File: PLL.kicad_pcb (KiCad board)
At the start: 2 copper layers, 100 x 70 mm, 43 parts, among them J1 Vout, J10 VpfdB2_tp, J11 Vsq_tp, J12 Vfb_tp, J13 Ven_tp, J14 Vref_tp, J2 M=1, J3 M=2, J4 M=4, J5 Vcp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

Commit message: FINISH
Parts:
- added G***: LOGO, LOGO, F.Cu at (69.5, 98.1)
- added REF**: MountingHole_3.2mm_M3_Pad_TopBottom, MountingHole:MountingHole_3.2mm_M3_Pad_TopBottom, F.Cu at (61.0, 108.0)
- added REF**: MountingHole_3.2mm_M3_Pad_TopBottom, MountingHole:MountingHole_3.2mm_M3_Pad_TopBottom, F.Cu at (153.9, 108.0)
- added REF**: MountingHole_3.2mm_M3_Pad_TopBottom, MountingHole:MountingHole_3.2mm_M3_Pad_TopBottom, F.Cu at (61.1, 45.0)
- added REF**: MountingHole_3.2mm_M3_Pad_TopBottom, MountingHole:MountingHole_3.2mm_M3_Pad_TopBottom, F.Cu at (153.9, 45.1)
- moved J12 127.4 mm to (73.6, 84.8)
- moved U2 101.5 mm to (103.6, 90.0)
- moved D4 98.5 mm to (102.9, 55.0)
- moved C3 89.5 mm to (125.2, 60.5), turned to -90 degrees
- moved D2 88.7 mm to (102.9, 66.0)
- moved D3 87.5 mm to (110.5, 59.5), turned to 180 degrees
- moved R7 86.4 mm to (146.5, 53.5), turned to -90 degrees
- moved C2 84.7 mm to (129.6, 58.5), turned to 90 degrees
- moved R6 81.4 mm to (154.3, 64.8), turned to 180 degrees
- moved J11 80.7 mm to (118.5, 79.5)
- moved J8 80.6 mm to (111.0, 79.5)
- moved R10 79.6 mm to (113.4, 53.8)
- moved R5 78.6 mm to (150.0, 61.1), turned to 90 degrees
- moved D1 78.2 mm to (110.5, 70.5), turned to 180 degrees
- moved R12 75.8 mm to (99.2, 61.4), turned to 90 degrees
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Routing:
- net VCC: track 0.00 -> 320.4 mm
- net Net-(J12-Pin_1): track 0.00 -> 69.6 mm, vias 0 -> 1
- net Net-(J1-Pin_1): track 0.00 -> 63.8 mm
- net Net-(J8-Pin_1): track 0.00 -> 63.0 mm
- net Net-(J14-Pin_1): track 0.00 -> 52.0 mm
- net Net-(J13-Pin_1): track 0.00 -> 48.1 mm
- net Net-(J5-Pin_1): track 0.00 -> 46.0 mm
- net Net-(J10-Pin_1): track 0.00 -> 45.9 mm, vias 0 -> 2
- net Net-(J9-Pin_1): track 0.00 -> 33.3 mm
- net Net-(J3-Pin_1): track 0.00 -> 29.8 mm
- net Net-(U1A-~{R}): track 0.00 -> 29.4 mm
- net Net-(J4-Pin_1): track 0.00 -> 28.4 mm
- net Net-(Q2-G): track 0.00 -> 26.1 mm
- net Net-(D1-A): track 0.00 -> 24.6 mm
- net Net-(U3A--): track 0.00 -> 21.0 mm
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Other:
- outline, holes or cut-outs redrawn
- board text added: "5V"
- board text added: "CP"
- board text added: "Design of Analog Electronic Systems - Final Assignment RF Synthesizer (PLL)"
- board text added: "Divider"
- board text added: "Loop Filter"
- board text added: "PFD"
- board text added: "Schmitt Trigger"
- board text added: "VCO"
- board text removed: "Design of Analog Electronic Systems - Final Assingment RF Synthesizer (PLL)"

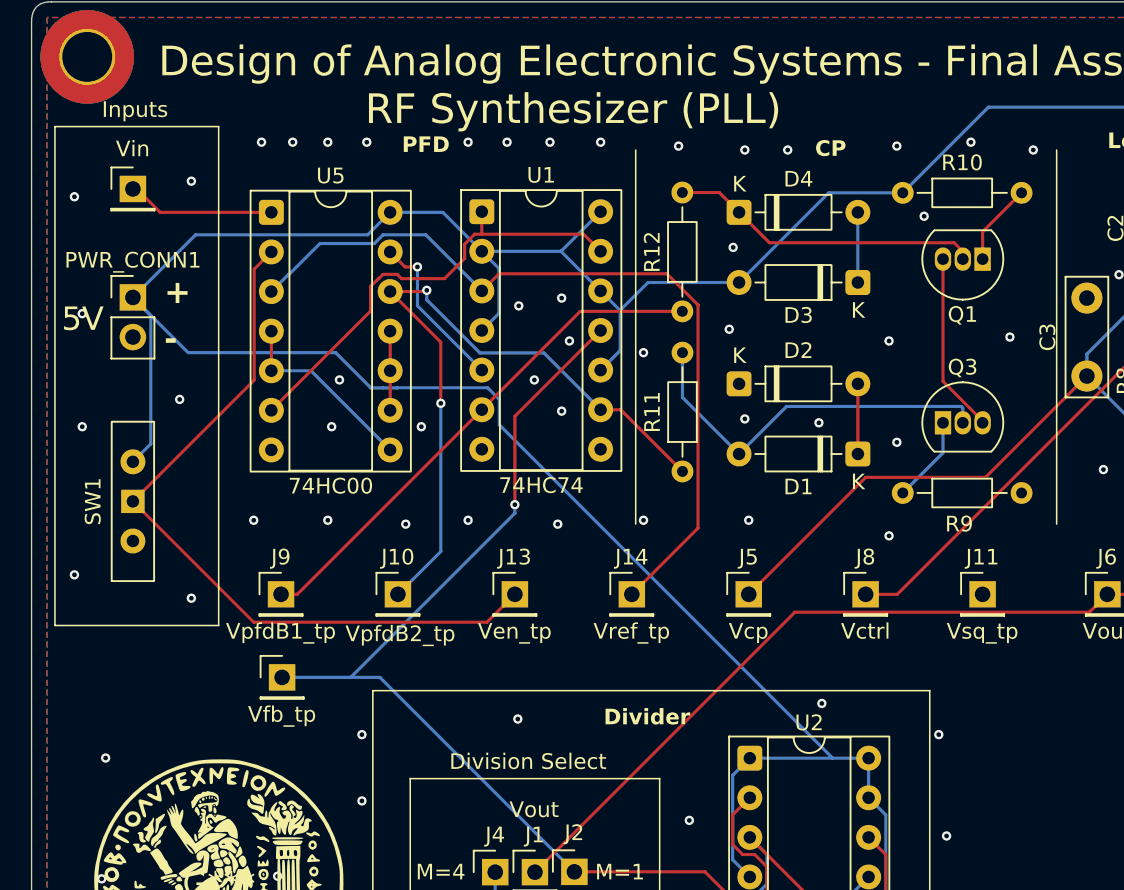
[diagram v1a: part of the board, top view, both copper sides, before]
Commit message: add LED indicator
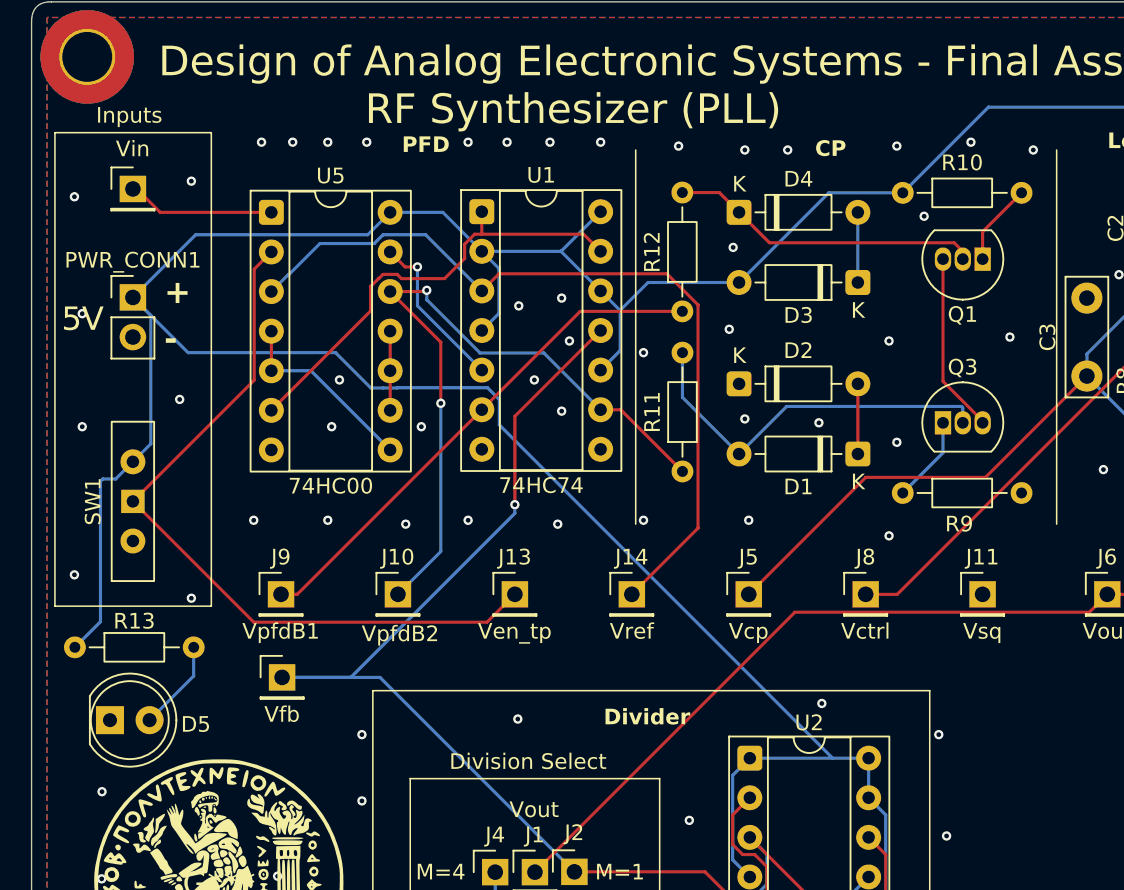
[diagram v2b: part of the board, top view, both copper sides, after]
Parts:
- added D5: LED, LED_THT:LED_D5.0mm, F.Cu at (62.5, 87.6)
- added R13: 330, Resistor_THT:R_Axial_DIN0204_L3.6mm_D1.6mm_P7.62mm_Horizontal, F.Cu at (60.3, 82.9)
- J10: value VpfdB2_tp -> VpfdB2
- J11: value Vsq_tp -> Vsq
- J12: value Vfb_tp -> Vfb
- J14: value Vref_tp -> Vref
- J9: value VpfdB1_tp -> VpfdB1
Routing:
- net VCC: track 320.4 -> 334.4 mm
- net Net-(D5-A): track 0.00 -> 5.84 mm

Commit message: Vsq connection fix
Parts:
- J13: value Ven_tp -> Ven
- renumbered PWR_CONN1 to PWR_HEADER1
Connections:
- J11 pad 1: unconnected-(J11-Pin_1-Pad1) -> Net-(J11-Pin_1)
- Q2 pad 2: Net-(Q2-G) -> Net-(J11-Pin_1)
- R3 pad 2: Net-(Q2-G) -> Net-(J11-Pin_1)
- U3 pad 1: Net-(Q2-G) -> Net-(J11-Pin_1)
- U4 pad 1: Net-(Q2-G) -> Net-(J11-Pin_1)
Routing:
- net Net-(J11-Pin_1): track 0.00 -> 51.9 mm
- net Net-(Q2-G): track 26.1 -> 0.00 mm
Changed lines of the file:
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@@
 	(net 8 "Net-(J1-Pin_1)")
 	(net 9 "Net-(J7-Pin_1)")
-	(net 10 "unconnected-(J11-Pin_1-Pad1)")
+	(net 10 "Net-(J11-Pin_1)")
 	(net 11 "Net-(J13-Pin_1)")
 	(net 12 "Net-(Q1-C)")
@@
 	(net 33 "Net-(U5-Pad10)")
 	(net 34 "Net-(Q2-D)")
-	(net 35 "Net-(Q2-G)")
-	(net 36 "Net-(D5-A)")
+	(net 35 "Net-(D5-A)")
 	(footprint "Connector_PinHeader_2.54mm:PinHeader_1x01_P2.54mm_Vertical"
 		(layer "F.Cu")
@@
 			(layers "*.Cu" "*.Mask")
 			(remove_unused_layers no)
-			(net 10 "unconnected-(J11-Pin_1-Pad1)")
+			(net 10 "Net-(J11-Pin_1)")
 			(pinfunction "Pin_1")
 			(pintype "passive")
@@
 		(descr "Through hole straight pin header, 1x02, 2.54mm pitch, single row")
 		(tags "Through hole pin header THT 1x02 2.54mm single row")
-		(property "Reference" "PWR_CONN1"
+		(property "Reference" "PWR_HEADER1"
 			(at 0 -2.38 0)
 			(layer "F.SilkS")
@@
 			)
 		)
-		(property "Value" "Ven_tp"
+		(property "Value" "Ven"
 			(at 0 2.38 0)
 			(layer "F.SilkS")
@@
 			(layers "*.Cu" "*.Mask")
 			(remove_unused_layers no)
-			(net 36 "Net-(D5-A)")
+			(net 35 "Net-(D5-A)")
 			(pinfunction "A")
 			(pintype "passive")
@@
 			(remove_unused_layers no)
 			(roundrect_rratio 0.15625)
-			(net 35 "Net-(Q2-G)")
+			(net 10 "Net-(J11-Pin_1)")
 			(pintype "input")
 		)
@@
 			(layers "*.Cu" "*.Mask")
 			(remove_unused_layers no)
-			(net 36 "Net-(D5-A)")
+			(net 35 "Net-(D5-A)")
 			(pintype "passive")
 		)
@@
 			(layers "*.Cu" "*.Mask")
 			(remove_unused_layers no)
-			(net 35 "Net-(Q2-G)")
+			(net 10 "Net-(J11-Pin_1)")
 			(pinfunction "G")
 			(pintype "input")
@@
 			(layers "*.Cu" "*.Mask")
 			(remove_unused_layers no)
-			(net 35 "Net-(Q2-G)")
+			(net 10 "Net-(J11-Pin_1)")
 			(pintype "passive")
 		)
@@
 			(remove_unused_layers no)
 			(roundrect_rratio 0.15625)
-			(net 35 "Net-(Q2-G)")
+			(net 10 "Net-(J11-Pin_1)")
 			(pintype "output")
 		)
@@
 	)
 	(segment
+		(start 141.25 73.75)
+		(end 141.25 69.05)
+		(width 0.2)
+		(layer "F.Cu")
+		(net 10)
+	)
+	(segment
+		(start 140.806 74.801)
+		(end 141.25 74.357)
+		(width 0.2)
+		(layer "F.Cu")
+		(net 10)
+	)
+	(segment
+		(start 141.25 73.75)
+		(end 141.25 73.975)
+		(width 0.2)
+		(layer "F.Cu")
+		(net 10)
+	)
+	(segment
+		(start 146.75 75.5)
+		(end 146.75 87.235)
+		(width 0.2)
+		(layer "F.Cu")
+		(net 10)
+	)
+	(segment
+		(start 146.75 87.235)
+		(end 144.735 89.25)
+		(width 0.2)
+		(layer "F.Cu")
+		(net 10)
+	)
+	(segment
+		(start 141.25 73.975)
+		(end 142.775 75.5)
+		(width 0.2)
+		(layer "F.Cu")
+		(net 10)
+	)
+	(segment
+		(start 139.154 74.801)
+		(end 140.806 74.801)
+		(width 0.2)
+		(layer "F.Cu")
+		(net 10)
+	)
+	(segment
+		(start 123.601 74.399)
+		(end 138.752 74.399)
+		(width 0.2)
+		(layer "F.Cu")
+		(net 10)
+	)
+	(segment
+		(start 142.775 75.5)
+		(end 146.75 75.5)
+		(width 0.2)
+		(layer "F.Cu")
+		(net 10)
+	)
+	(segment
+		(start 141.25 74.357)
+		(end 141.25 73.75)
+		(width 0.2)
+		(layer "F.Cu")
+		(net 10)
+	)
+	(segment
+		(start 141.25 69.05)
+		(end 141.56 68.74)
+		(width 0.2)
+		(layer "F.Cu")
+		(net 10)
+	)
+	(segment
+		(start 118.5 79.5)
+		(end 123.601 74.399)
+		(width 0.2)
+		(layer "F.Cu")
+		(net 10)
+	)
+	(segment
+		(start 138.752 74.399)
+		(end 139.154 74.801)
+		(width 0.2)
+		(layer "F.Cu")
+		(net 10)
+	)
+	(segment
 		(start 71.779 58.641)
 		(end 72.88 57.54)
@@
 	)
 	(segment
-		(start 141.25 73.75)
-		(end 141.25 69.05)
-		(width 0.2)
-		(layer "F.Cu")
-		(net 35)
-	)
-	(segment
-		(start 141.25 73.75)
-		(end 141.25 73.975)
-		(width 0.2)
-		(layer "F.Cu")
-		(net 35)
-	)
-	(segment
-		(start 146.75 75.5)
-		(end 146.75 87.235)
-		(width 0.2)
-		(layer "F.Cu")
-		(net 35)
-	)
-	(segment
-		(start 146.75 87.235)
-		(end 144.735 89.25)
-		(width 0.2)
-		(layer "F.Cu")
-		(net 35)
-	)
-	(segment
-		(start 141.25 73.975)
-		(end 142.775 75.5)
-		(width 0.2)
-		(layer "F.Cu")
-		(net 35)
-	)
-	(segment
-		(start 142.775 75.5)
-		(end 146.75 75.5)
-		(width 0.2)
-		(layer "F.Cu")
-		(net 35)
-	)
-	(segment
-		(start 141.25 69.05)
-		(end 141.56 68.74)
-		(width 0.2)
-		(layer "F.Cu")
-		(net 35)
-	)
-	(segment
 		(start 67.9 82.9)
 		(end 67.9 84.74)
 		(width 0.2)
 		(layer "B.Cu")
-		(net 36)
+		(net 35)
 	)
 	(segment
@@
 		(width 0.2)
 		(layer "B.Cu")
-		(net 36)
+		(net 35)
 	)
 	(zone
